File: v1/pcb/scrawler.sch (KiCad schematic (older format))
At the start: 72 parts, among them J2 MJ-4PP-9, J3 OLED, SW1 SW_PUSH, SW10 SW_PUSH, SW11 SW_PUSH, SW12 SW_PUSH, SW13 SW_PUSH, SW14 SW_PUSH, SW15 SW_PUSH, SW16 SW_PUSH, SW17 SW_PUSH, SW18 SW_PUSH, SW19 SW_PUSH, SW2 SW_PUSH, SW20 SW_PUSH, SW21 SW_PUSH, SW22 SW_PUSH, SW23 SW_PUSH, SW24 SW_PUSH, SW25 SW_PUSH, SW26 Rotary_Encoder_Switch, SW3 SW_PUSH, SW4 SW_PUSH, SW5 SW_PUSH, SW6 SW_PUSH, SW7 SW_PUSH, SW8 SW_PUSH, SW9 SW_PUSH, U1 ProMicro

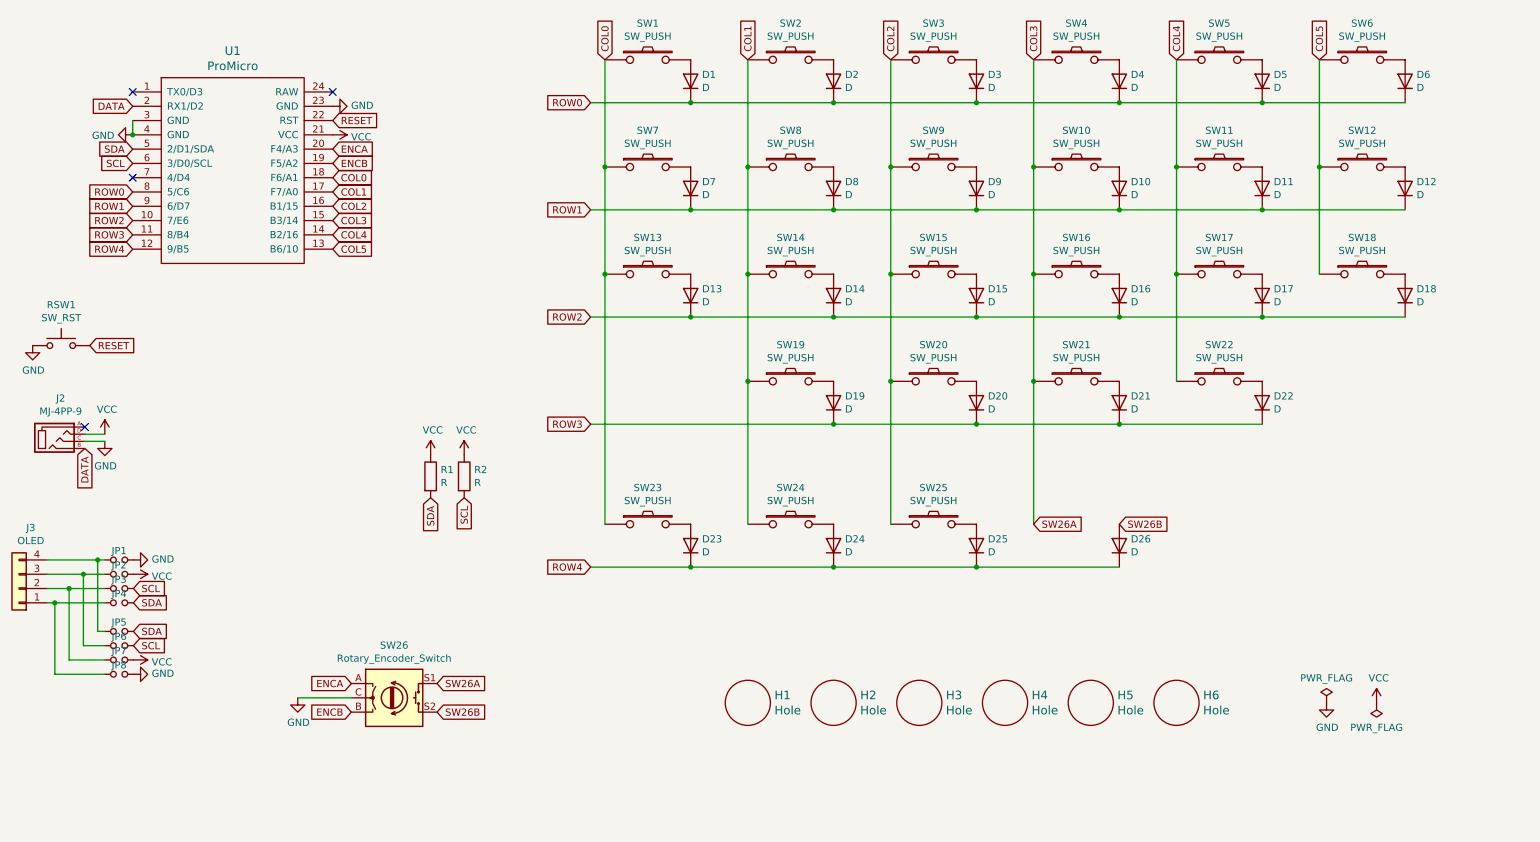
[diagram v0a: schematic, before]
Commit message: assigned footprints
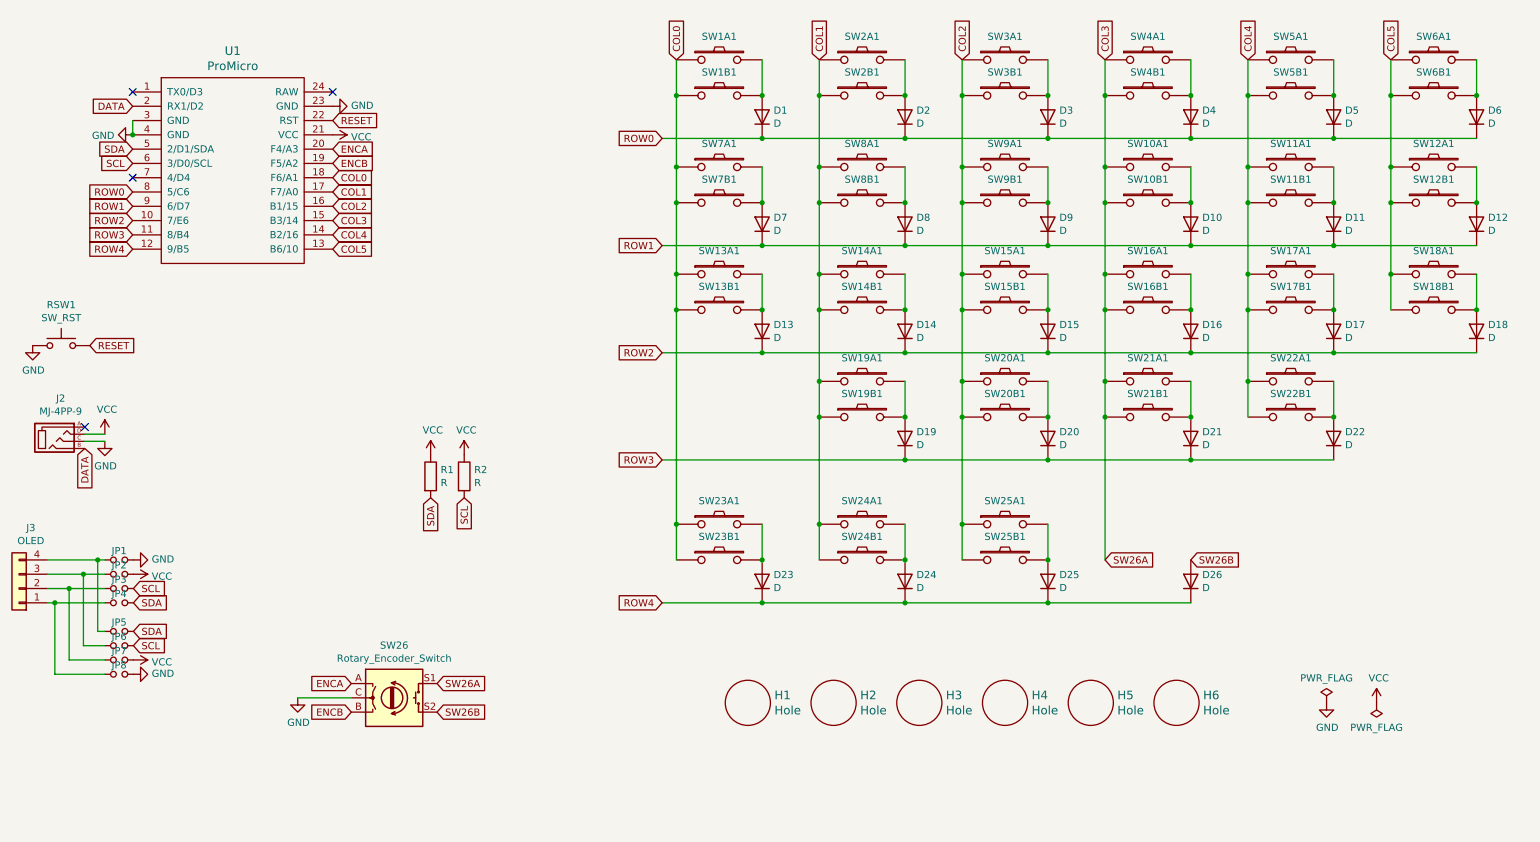
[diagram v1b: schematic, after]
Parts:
- removed SW1, SW10, SW11, SW12, SW13, SW14, SW15, SW16, SW17, SW18, SW19, SW2, SW20, SW21, SW22, SW23, SW24, SW25, SW3, SW4, SW5, SW6, SW7, SW8, SW9: SW_PUSH, symbol kbd:SW_PUSH
- added SW10A1, SW11A1, SW12A1, SW13A1, SW14A1, SW15A1, SW16A1, SW17A1, SW18A1, SW19A1, SW1A1, SW20A1, SW21A1, SW22A1, SW23A1, SW24A1, SW25A1, SW2A1, SW3A1, SW4A1, SW5A1, SW6A1, SW7A1, SW8A1, SW9A1: SW_PUSH, keyswitches:MX_reversible, symbol kbd:SW_PUSH
- added SW10B1, SW11B1, SW12B1, SW13B1, SW14B1, SW15B1, SW16B1, SW17B1, SW18B1, SW19B1, SW1B1, SW20B1, SW21B1, SW22B1, SW23B1, SW24B1, SW25B1, SW2B1, SW3B1, SW4B1, SW5B1, SW6B1, SW7B1, SW8B1, SW9B1: SW_PUSH, keyswitches:PG1350_socket_reversible, symbol kbd:SW_PUSH
- D1, D10, D11, D12, D13, D14, D15, D16, D17, D18, D19, D2, D20, D21, D22, D23, D24, D25, D26, D3, D4, D5, D6, D7, D8, D9: footprint (none) -> SofleKeyboard-footprint:Diode_SOD123
- H1, H2, H3, H4, H5, H6: footprint (none) -> SofleKeyboard-footprint:HOLE_M2_TH
- J2: footprint (none) -> SofleKeyboard-footprint:MJ-4PP-9
- J3: footprint (none) -> SofleKeyboard-footprint:OLED_4Pin
- JP1, JP2, JP3, JP4, JP5, JP6, JP7, JP8: footprint (none) -> SofleKeyboard-footprint:Jumper
- R1, R2: footprint (none) -> SofleKeyboard-footprint:R_1206_DoubleSided
- RSW1: footprint (none) -> footprints:SW_PUSH_6mm
- SW26: footprint (none) -> SofleKeyboard-footprint:RotaryEncoder_Alps_EC11E-Switch_Vertical_H20mm-keebio_modified
- U1: footprint (none) -> Keebio-Parts:ArduinoProMicro
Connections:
- net COL0: now also SW13A1.1, SW13B1.1, SW1A1.1, SW1B1.1, SW23A1.1, SW23B1.1, SW7A1.1, SW7B1.1
- net COL1: now also SW14A1.1, SW14B1.1, SW19A1.1, SW19B1.1, SW24A1.1, SW24B1.1, SW2A1.1, SW2B1.1, SW8A1.1, SW8B1.1
- net COL2: now also SW15A1.1, SW15B1.1, SW20A1.1, SW20B1.1, SW25A1.1, SW25B1.1, SW3A1.1, SW3B1.1, SW9A1.1, SW9B1.1
- net COL3: now also SW10A1.1, SW10B1.1, SW16A1.1, SW16B1.1, SW21A1.1, SW21B1.1, SW4A1.1, SW4B1.1
- net COL4: now also SW11A1.1, SW11B1.1, SW17A1.1, SW17B1.1, SW22A1.1, SW22B1.1, SW5A1.1, SW5B1.1
- net COL5: now also SW12A1.1, SW12B1.1, SW18A1.1, SW18B1.1, SW6A1.1, SW6B1.1
- net at D1.2 (A): now also SW1A1.2, SW1B1.2
- net at D7.2 (A): now also SW7A1.2, SW7B1.2
- net at D13.2 (A): now also SW13A1.2, SW13B1.2
- net at D2.2 (A): now also SW2A1.2, SW2B1.2
- net at D8.2 (A): now also SW8A1.2, SW8B1.2
- net at D14.2 (A): now also SW14A1.2, SW14B1.2
- net at D19.2 (A): now also SW19A1.2, SW19B1.2
- net at D3.2 (A): now also SW3A1.2, SW3B1.2
- net at D9.2 (A): now also SW9A1.2, SW9B1.2
- net at D15.2 (A): now also SW15A1.2, SW15B1.2
- net at D20.2 (A): now also SW20A1.2, SW20B1.2
- net at D4.2 (A): now also SW4A1.2, SW4B1.2
- net at D10.2 (A): now also SW10A1.2, SW10B1.2
- net at D16.2 (A): now also SW16A1.2, SW16B1.2
- net at D21.2 (A): now also SW21A1.2, SW21B1.2
- net at D5.2 (A): now also SW5A1.2, SW5B1.2
- net at D11.2 (A): now also SW11A1.2, SW11B1.2
- net at D17.2 (A): now also SW17A1.2, SW17B1.2
- net at D22.2 (A): now also SW22A1.2, SW22B1.2
- net at D6.2 (A): now also SW6A1.2, SW6B1.2
- net at D12.2 (A): now also SW12A1.2, SW12B1.2
- net at D18.2 (A): now also SW18A1.2, SW18B1.2
- net at D23.2 (A): now also SW23A1.2, SW23B1.2
- net at D24.2 (A): now also SW24A1.2, SW24B1.2
- net at D25.2 (A): now also SW25A1.2, SW25B1.2

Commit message: placed main switches in physical pcb
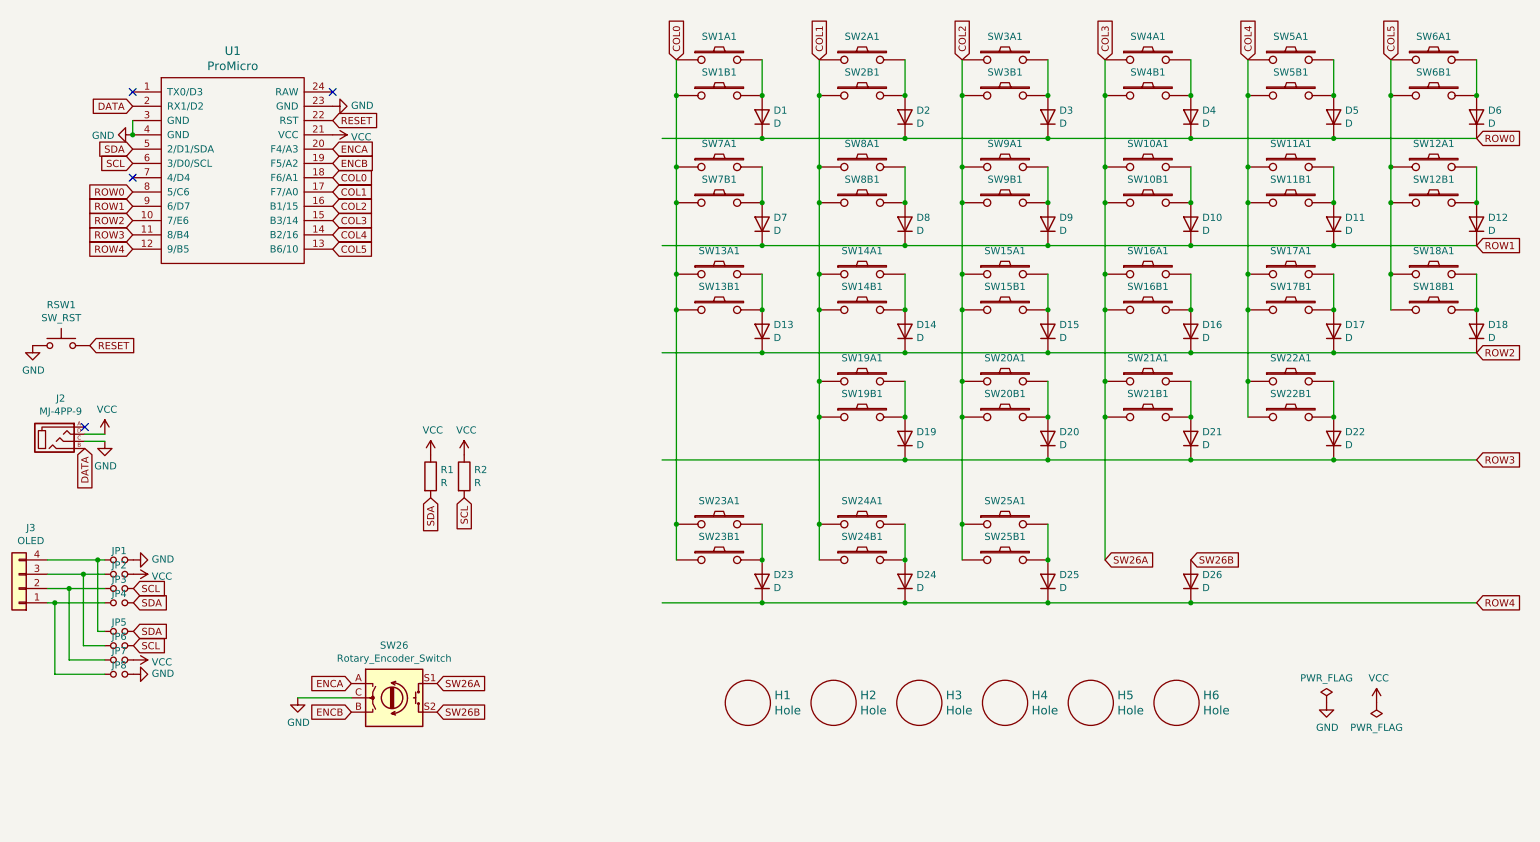
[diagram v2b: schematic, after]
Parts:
- J2: footprint SofleKeyboard-footprint:MJ-4PP-9 -> kbd:MJ-4PP-9
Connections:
- wire segments 116 -> 118
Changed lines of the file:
@@
 F 0 "J2" H 1191 4421 50  0000 C CNN
 F 1 "MJ-4PP-9" H 1191 4330 50  0000 C CNN
-F 2 "SofleKeyboard-footprint:MJ-4PP-9" H 1435 4320 50  0001 C CNN
+F 2 "kbd:MJ-4PP-9" H 1435 4320 50  0001 C CNN
 F 3 "~" H 1435 4320 50  0001 C CNN
 	1    1160 4145
@@
 Text GLabel 10500 1500 1    50   Input ~ 0
 COL5
-Text GLabel 5400 2050 0    50   Input ~ 0
+Text GLabel 11100 2050 2    50   Input ~ 0
 ROW0
-Text GLabel 5400 2800 0    50   Input ~ 0
+Text GLabel 11100 2800 2    50   Input ~ 0
 ROW1
-Text GLabel 5400 3550 0    50   Input ~ 0
+Text GLabel 11100 3550 2    50   Input ~ 0
 ROW2
-Text GLabel 5400 4300 0    50   Input ~ 0
+Text GLabel 11100 4300 2    50   Input ~ 0
 ROW3
-Text GLabel 5400 5300 0    50   Input ~ 0
+Text GLabel 11100 5300 2    50   Input ~ 0
 ROW4
 Text GLabel 1695 1825 0    50   Input ~ 0
@@
 	1    0    0    -1
 $EndComp
+Wire Wire Line
+	10100 4300 11100 4300
+Connection ~ 10100 4300
+Wire Wire Line
+	9100 5300 11100 5300
+Connection ~ 9100 5300
 $EndSCHEMATC

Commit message: pcb done
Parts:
- added H7, H8: Hole, SofleKeyboard-footprint:M2_HOLE_PCB, symbol keebio:Hole
- renumbered SW23A1 to SW24A1, SW23B1 to SW24B1, SW24A1 to SW25A1, SW24B1 to SW25B1, SW25A1 to SW26A1, SW25B1 to SW26B1
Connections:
- net labels added: SW23A, SW23B
- net labels removed: SW26A, SW26B
- wire segments 118 -> 115
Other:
- moved on the sheet: D23, D24, D25, D26, SW24A1, SW24B1, SW25A1, SW25B1, SW26A1, SW26B1

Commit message: generated gerber files
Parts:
- renumbered SW26 to SW23
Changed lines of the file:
@@
 $EndComp
 $Comp
-L Device:Rotary_Encoder_Switch SW26
+L Device:Rotary_Encoder_Switch SW23
 U 1 1 6122561E
 P 3525 5965
-F 0 "SW26" H 3525 6332 50  0000 C CNN
+F 0 "SW23" H 3525 6332 50  0000 C CNN
 F 1 "Rotary_Encoder_Switch" H 3525 6241 50  0000 C CNN
 F 2 "SofleKeyboard-footprint:RotaryEncoder_Alps_EC11E-Switch_Vertical_H20mm-keebio_modified" H 3375 6125 50  0001 C CNN
